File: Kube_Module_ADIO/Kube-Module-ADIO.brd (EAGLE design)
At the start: 42.8 x 54.6 mm, 13 parts, among them IC1 MCP23017SP

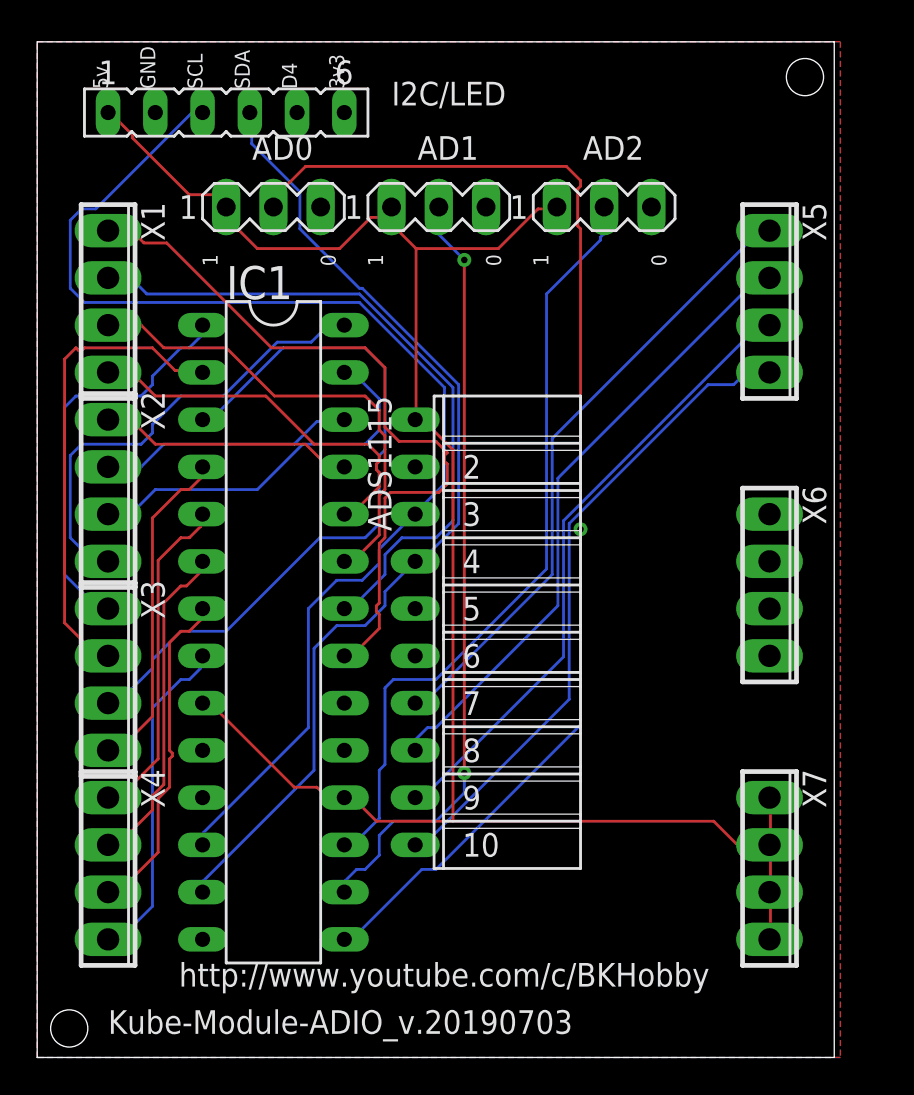
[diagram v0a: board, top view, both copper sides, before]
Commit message: Mods to ADIO to add add'l GND pins and space TBs better.
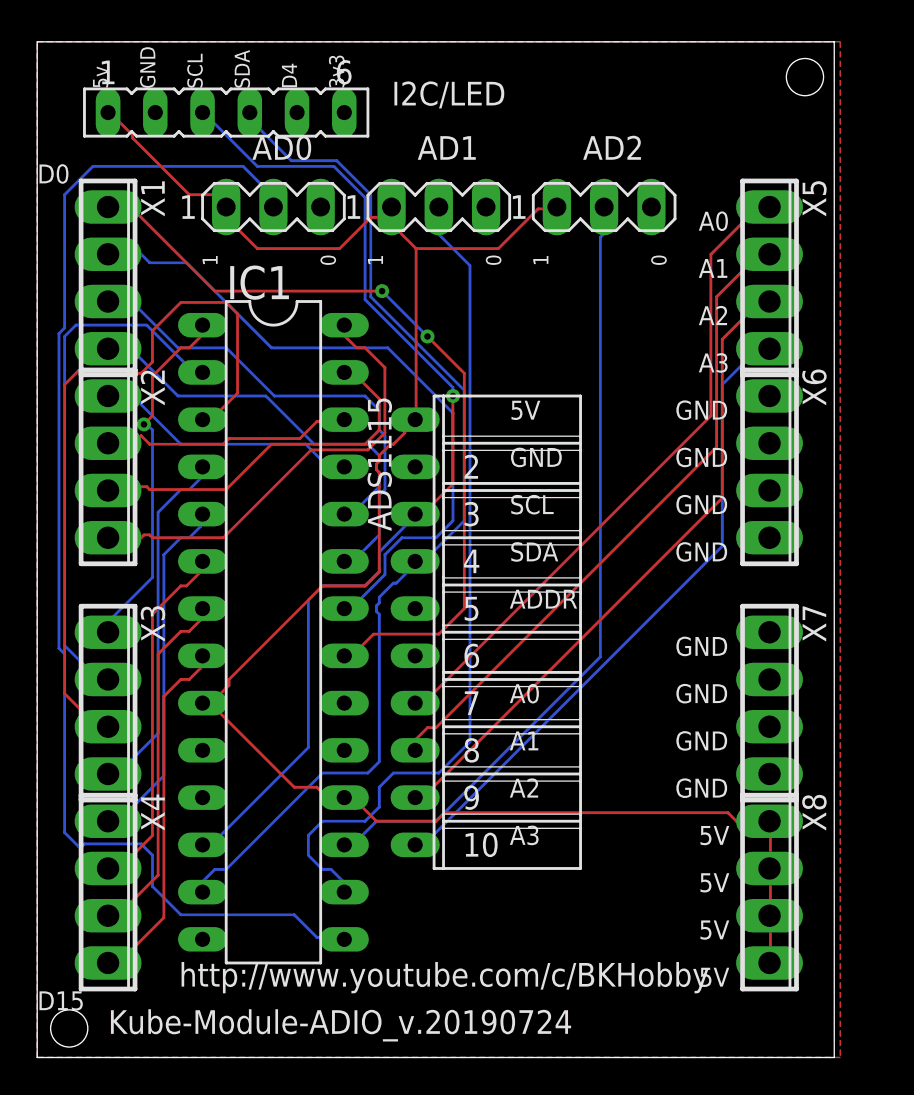
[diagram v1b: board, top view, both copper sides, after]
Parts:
- added X8: (no value), con-phoenix-254:4POL254
- moved X7 8.89 mm to (55.9, 29.2)
- moved X6 6.35 mm to (55.9, 41.9)
- moved X1 1.27 mm to (20.3, 52.1)
- moved X5 1.27 mm to (55.9, 52.1)
- moved X3 1.27 mm to (20.3, 29.2)
- moved X4 1.27 mm to (20.3, 19.1)
- moved X2 1.27 mm to (20.3, 41.9)
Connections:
- net 5V: now also X8.1, X8.2, X8.3, X8.4; no longer X7.1, X7.2, X7.3, X7.4
- net GND: now also X7.1, X7.2, X7.3, X7.4
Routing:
- net SCL(D1): track 66.3 -> 54.9 mm, vias 0 -> 1
- net AD1: track 41.7 -> 45.0 mm, vias 2 -> 0
- net SDA(D2): track 53.5 -> 56.3 mm
- net D9: track 25.6 -> 28.4 mm
- net D0: track 40.3 -> 43.0 mm, vias 0 -> 2
- net D8: track 22.0 -> 19.4 mm, vias 0 -> 1
- net D13: track 17.8 -> 19.1 mm
- net A0: track 33.8 -> 35.2 mm
- net AD0: track 64.9 -> 66.2 mm, vias 1 -> 0
- net D15: track 18.0 -> 19.2 mm
- net D12: track 18.0 -> 19.2 mm
- net A1: track 33.9 -> 35.2 mm
- net D11: track 18.0 -> 19.2 mm
- net A2: track 33.9 -> 35.1 mm
- net D14: track 18.1 -> 19.2 mm
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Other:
- board text added: "Kube-Module-ADIO_v.20190724"
- board text removed: "Kube-Module-ADIO_v.20190703"

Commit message: Added ADS1115 addressing jumper
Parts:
- added AADRR: (no value), con-lstb:MA04-2
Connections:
- new net ADDR: AADRR.2, AADRR.4, AADRR.6, AADRR.8, ADS1115.5
- net 5V: now also AADRR.3
- net GND: now also AADRR.1; no longer ADS1115.5
- net SCL(D1): now also AADRR.7
- net SDA(D2): now also AADRR.5
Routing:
- net ADDR: track 0.00 -> 24.6 mm
- net AD1: track 45.0 -> 62.2 mm, vias 0 -> 1
- net SDA(D2): track 56.3 -> 67.2 mm
- net 5V: track 103.7 -> 112.0 mm
- net SCL(D1): track 54.9 -> 62.6 mm, vias 1 -> 0
- net AD2: track 42.2 -> 45.4 mm
- net D0: track 43.0 -> 45.3 mm, vias 2 -> 1
- net D1: track 36.3 -> 36.6 mm, vias 0 -> 1
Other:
- board text added: "48"
- board text added: "49"
- board text added: "4A"
- board text added: "4B"
- board text added: "Kube-Module-ADIO_v.20210404"
- board text removed: "Kube-Module-ADIO_v.20190724"
